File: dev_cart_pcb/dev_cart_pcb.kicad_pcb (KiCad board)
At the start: 2 copper layers, 60 x 78 mm, 3 parts, among them J1 GGPins, J2 Conn_01x23, J3 Conn_01x22

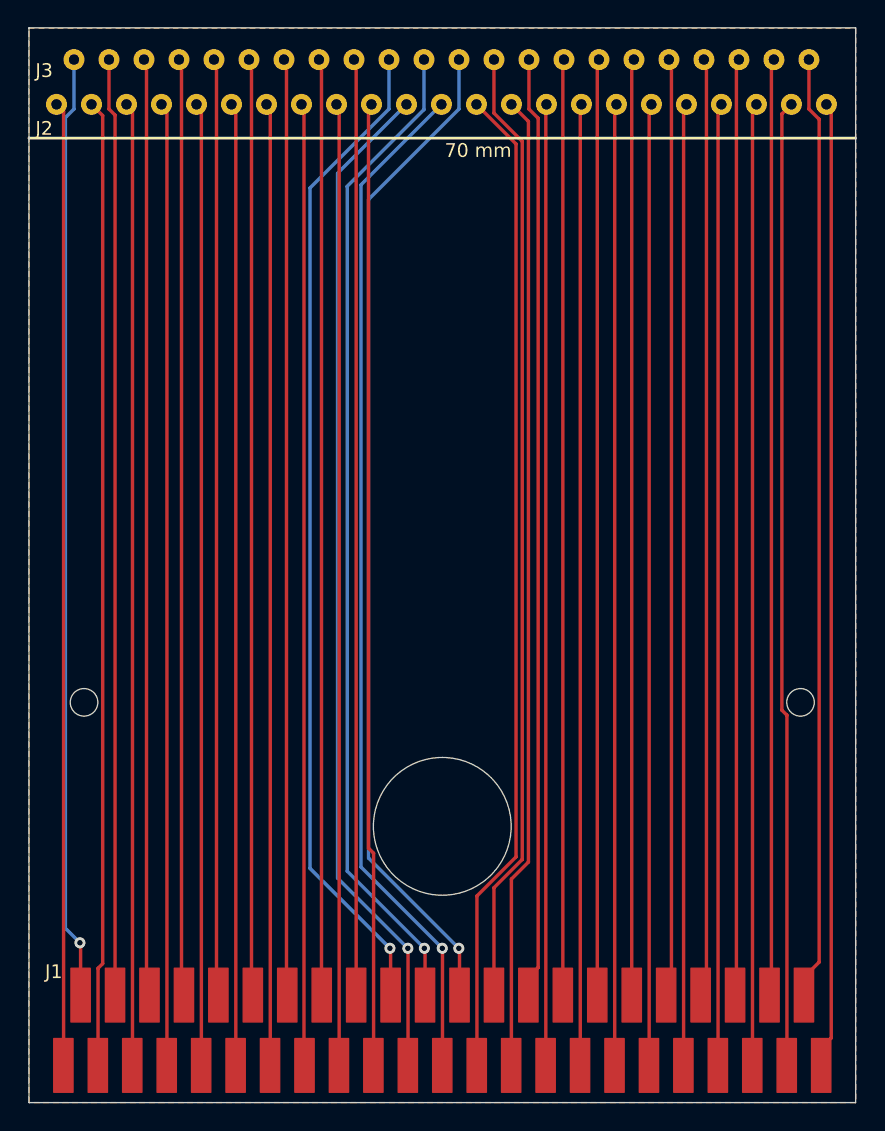
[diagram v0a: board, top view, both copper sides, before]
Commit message: Added gg-card-dimensions.svg, an Inkscape SVG of a GG cartridge PCB.
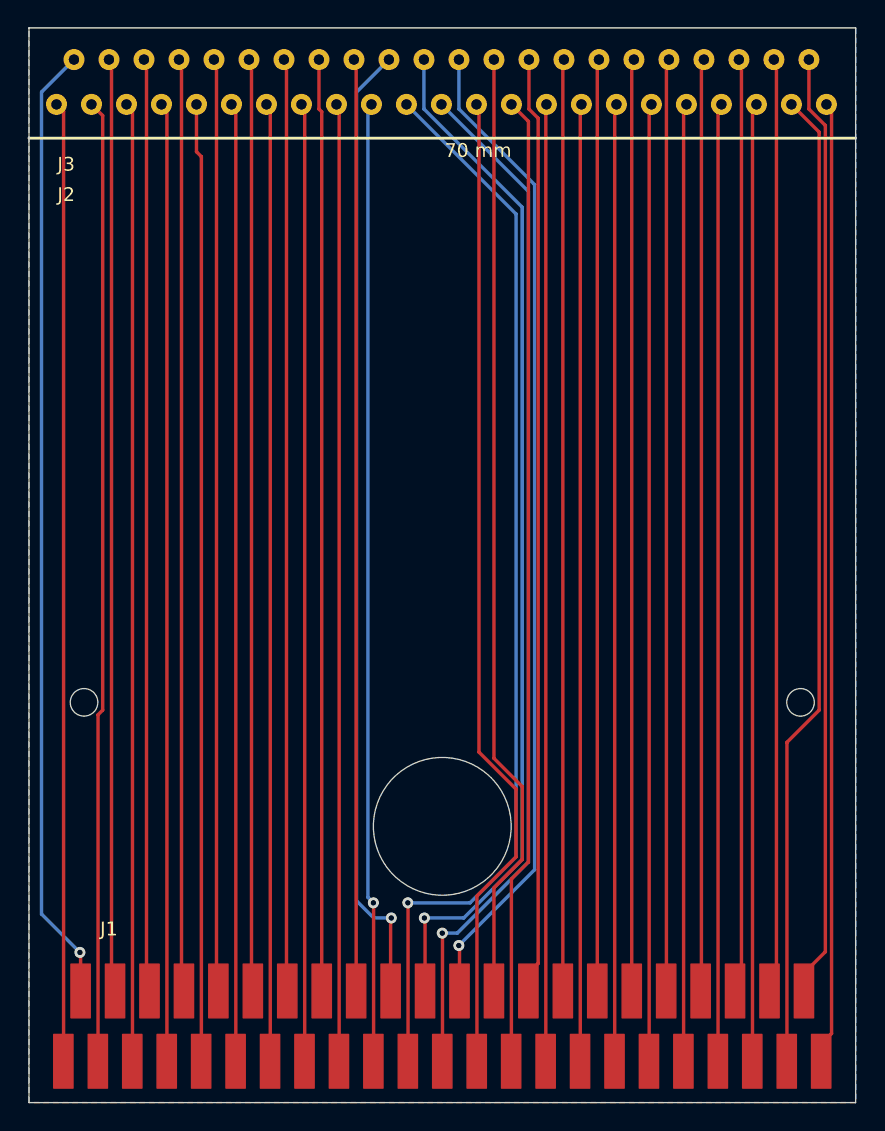
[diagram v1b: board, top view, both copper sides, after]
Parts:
- moved J1 0.30 mm to (74.3, 111.2)
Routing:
- net Net-(J1-Pad21): track 72.7 -> 77.4 mm
- net Net-(J1-Pad22): track 71.3 -> 73.9 mm
- net Net-(J1-Pad20): track 71.4 -> 69.1 mm
- net Net-(J1-Pad24): track 72.1 -> 70.9 mm
- net Net-(J1-Pad2): track 67.3 -> 68.5 mm
- net Net-(J1-Pad43): track 68.9 -> 70.0 mm
- net Net-(J1-Pad12): track 66.7 -> 67.5 mm
- net Net-(J1-Pad23): track 73.3 -> 74.0 mm
- net Net-(J1-Pad19): track 68.7 -> 68.8 mm, vias 0 -> 1
